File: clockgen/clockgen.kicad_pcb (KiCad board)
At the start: 2 copper layers, 55 x 21 mm, 10 parts, among them J1 Conn_01x03_Male, J2 Conn_01x05_Male, Q101 BC847, U1 ATtiny13A-P

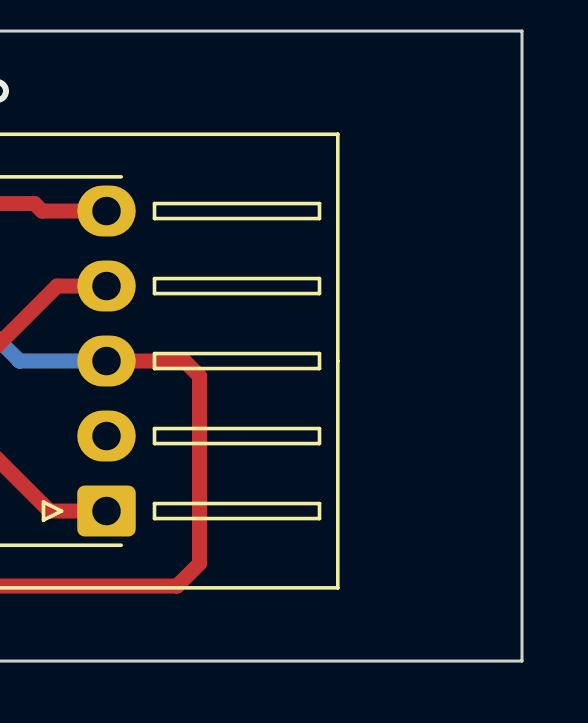
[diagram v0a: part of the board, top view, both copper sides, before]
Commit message: added pin description for J2
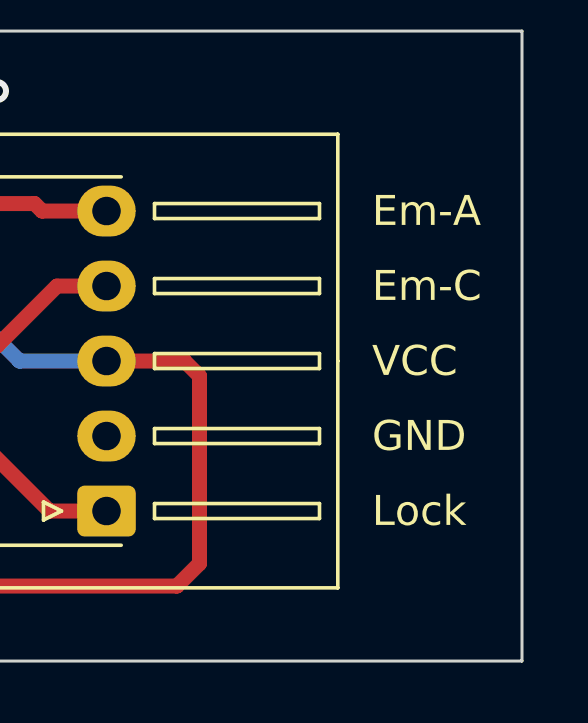
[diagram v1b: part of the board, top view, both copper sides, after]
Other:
- board text added: "Em-A"
- board text added: "Em-C"
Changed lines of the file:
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@@
 		(layer "Edge.Cuts")
+	)
+	(gr_text "Em-C"
+		(at 159.5 93.5 0)
+		(layer "F.SilkS")
+		(effects
+			(font
+				(size 1 1)
+				(thickness 0.1)
+			)
+			(justify left)
+		)
+	)
+	(gr_text "Lock"
+		(at 159.5 101 0)
+		(layer "F.SilkS")
+		(effects
+			(font
+				(size 1 1)
+				(thickness 0.1)
+			)
+			(justify left)
+		)
 	)
 	(gr_text "VCC"
@@
 		)
 	)
+	(gr_text "Em-A"
+		(at 159.5 91 0)
+		(layer "F.SilkS")
+		(effects
+			(font
+				(size 1 1)
+				(thickness 0.1)
+			)
+			(justify left)
+		)
+	)
+	(gr_text "GND"
+		(at 159.5 98.5 0)
+		(layer "F.SilkS")
+		(effects
+			(font
+				(size 1 1)
+				(thickness 0.1)
+			)
+			(justify left)
+		)
+	)
+	(gr_text "VCC"
+		(at 159.5 96 0)
+		(layer "F.SilkS")
+		(effects
+			(font
+				(size 1 1)
+				(thickness 0.1)
+			)
+			(justify left)
+		)
+	)

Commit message: cleanup
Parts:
- moved J1 24.1 mm to (128.4, 69.5)
- moved U1 24.0 mm to (134.4, 64.7)
- moved C1 24.0 mm to (146.7, 63.2)
- moved D2 24.0 mm to (146.2, 73.4)
- moved Q101 24.0 mm to (138.2, 77.2)
- moved R1 24.0 mm to (127.2, 64.0)
- moved R2 24.0 mm to (145.9, 67.0)
- moved R3 24.0 mm to (132.4, 77.0)
- moved R4 24.0 mm to (145.4, 79.7)
- moved J2 23.9 mm to (151.8, 77.1)
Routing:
- net Lock: track 38.1 -> 34.1 mm
- net Emitter1-Cathode: track 18.3 -> 16.7 mm
- net Emitter1-Anode: track 7.50 -> 5.88 mm
- net VCC: track 64.2 -> 64.9 mm
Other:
- board text removed: "Em-A"
- board text removed: "Em-C"
- board text removed: "GND"
- board text removed: "Lock"
- board text removed: "VCC"
